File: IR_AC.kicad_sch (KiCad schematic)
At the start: 1 part

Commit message: late night work on led current
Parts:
- added C1, C2: 1u, Capacitor_SMD:C_0603_1608Metric, symbol Device:C
- added CLDO1, CLDO2: 1u, Capacitor_SMD:C_0805_2012Metric, symbol Device:C
- added D1: 1N5819HW, LC_libz_foot:1N5819HW, symbol Device:D_Schottky
- added D2, D3: RED_GREEN, LED_SMD:LED_0805_2012Metric, symbol Device:LED
- added D4: LED, LC_libz_foot:IR_LED_TH_5MM, symbol Device:LED
- added D5: RED, LED_SMD:LED_0805_2012Metric, symbol Device:LED
- added H1, H2, H3, H4: MountingHole, MountingHole:MountingHole_3.2mm_M3, symbol Mechanical:MountingHole
- added J1: TYPE-C 16PIN 2MD(073), LC_libz_foot:USB-C-SMD_TYPE-C-6PIN-2MD-073, symbol LC_libz_sym:TYPE-C16PIN2MD(073)
- added Q1: NMOS, Package_TO_SOT_SMD:SOT-23, symbol Simulation_SPICE:NMOS
- added R2: 10k, Resistor_SMD:R_0603_1608Metric, symbol Device:R
- added R3: 100R, Resistor_SMD:R_0603_1608Metric, symbol Device:R
- added R4: 100k, Resistor_SMD:R_0603_1608Metric, symbol Device:R
- added R?: 3k3, Resistor_SMD:R_0603_1608Metric, symbol Device:R
- added R?: 220R, Resistor_SMD:R_0603_1608Metric, symbol Device:R
- added R?: 820R, Resistor_SMD:R_0603_1608Metric, symbol Device:R
- added R?: 33R, Resistor_SMD:R_1206_3216Metric, symbol Device:R
- added RCC1, RCC2: 5.1k, Resistor_SMD:R_0603_1608Metric, symbol Device:R
- added SW1, SW2: SW_Push, LC_libz_foot:BTN_L45_W45, symbol Switch:SW_Push
- added TP1, TP2, TP3: TestPoint, TestPoint:TestPoint_THTPad_D1.5mm_Drill0.7mm, symbol Connector:TestPoint
- added U1: AP2112K-3.3TRG1, LC_libz_foot:AP2112K-3.3, symbol LC_libz_sym:AP2112K-3.3TRG1
- added U2: WS2812B_5050, LC_libz_foot:WS2812B_5050, symbol LC_libz_sym:WS2812B_5050
- added U3: ESP32-S3-WROOM-1, RF_Module:ESP32-S3-WROOM-1, symbol RF_Module:ESP32-S3-WROOM-1
- R1: LCSC C2930027 -> C25804
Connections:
- net +5V: now also CLDO1.1, D1.1 (K), R?.2, R?.2, R?.2, U1.1 (VIN), U1.3 (EN); no longer R1.1
- net GND: now also C1.2, C2.2, CLDO1.2, CLDO2.2, D2.1 (K), D3.1 (K), J1.1 (GND), J1.12 (GND), Q1.3 (S), R4.1, RCC1.1, RCC2.1, SW1.1, SW2.1, U1.2 (GND), U2.3 (GND), U3.1 (GND), U3.40 (GND), U3.41 (GND); no longer R1.2
- new net: D3.2 (A), R?.1, TP2.1
- new net: D5.2 (A), R?.1
- new net: D2.2 (A), R?.1, TP1.1
- new net: J1.10 (CC2), RCC2.2
- new net: J1.4 (CC1), RCC1.2
- new net: D4.1 (K), D5.1 (K), Q1.1 (D)
- new net: Q1.2 (G), R3.1, R4.2
- new net: D4.2 (A), R?.1, TP3.1
- new net +3V3: CLDO2.1, R1.2, R2.2, R?.2, U1.5 (VOUT), U3.2 (3V3)
- new net BOOT: C2.1, R2.1, SW2.2, U3.27 (IO0)
- new net D+: J1.6 (DP1), J1.8 (DP2), U3.14 (USB_D+)
- new net D-: J1.5 (DN2), J1.7 (DN1), U3.13 (USB_D-)
- new net EN: C1.1, R1.1, SW1.2, U3.3 (EN)
- new net IR_LED_DRIVE: R3.2
- new net LED_STATUS: U2.1 (VDD)
- new net VDC: D1.2 (A), J1.11 (VBUS), J1.2 (VBUS)
- no-connect marks 0 -> 6
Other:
- note added: "Assuming IR LED pulses of 100mA, the R_DS(on) of the NMOS (2N7002) will cause a V_DS drop of ~0.4V. At this current the IR LED will drop about 1.3V. Hence, the current- limiting resistor is calculated as: R_IR-LED = (5-1.3-0.4)/0.1 = 33R ..and power P = (0.1)^2 * (33) = 0.33 W => 1206"
- note added: "EN-RESET / BOOT BUTTONS"
- note added: "Fixed 3V3 LDO (efficient, not monolithic AMS1117)"
- note added: "Hence, more like 4.55V"
- note added: "IR Blaster"
- note added: "IR TX LED (940nm) 5mm THT"
- note added: "Ideally differentially routed but only short. Z_0 = 90R."
- note added: "Indicator LEDs"
- note added: "Mounting Holes"
- note added: "Schottky reverse polarity protection"
- note added: "Strapping pins copied from ESP32-S3 DevKitC-1 schematic"
- note added: "Tandem visible spectrum LED to indicate TX"
- note added: "USB-C 16P Receptacle (power + data)"
- note added: "V_F = 0.45V @ 1A"
- note added: "WS2812B RGB Status LED"

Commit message: Finished schematic
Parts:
- added C1, C4: 10u, Capacitor_SMD:C_0805_2012Metric, symbol Device:C
- added C5: 100n, Capacitor_SMD:C_0402_1005Metric, symbol Device:C
- added D4: YELLOW, LED_SMD:LED_0805_2012Metric, symbol Device:LED
- added J2: Conn_01x04_Pin, libs:HDR-TH_4P-P2.54-V-M, symbol Connector:Conn_01x04_Pin
- added R3: 1k, Resistor_SMD:R_0603_1608Metric, symbol Device:R
- added TP3: TestPoint, TestPoint:TestPoint_THTPad_D1.5mm_Drill0.7mm, symbol Connector:TestPoint
- added U2: USBLC6-4, Package_TO_SOT_SMD:SOT-23-6, symbol Power_Protection:SRV05-4
- D2, D3: value RED_GREEN -> GREEN
- D6: renamed from D5; LCSC NULL -> C84256
- H1, H2, H3, H4: footprint MountingHole:MountingHole_3.2mm_M3 -> MountingHole:MountingHole_2.2mm_M2
- J1: footprint LC_libz_foot:USB-C-SMD_TYPE-C-6PIN-2MD-073 -> libs:USB-C-SMD_TYPE-C-6PIN-2MD-073
- R1: renamed from R?; value 220R -> 680R; LCSC C22962 -> C23228
- R2: renamed from R?; value 820R -> 2k2; LCSC C23253 -> C4190
- R6: renamed from R?; value 33R -> 30R; LCSC C18005 -> C25373
- R7: renamed from R?; value 3k3 -> 330R; LCSC C22978 -> C23138
- SW1, SW2: footprint LC_libz_foot:BTN_L45_W45 -> (none); LCSC C455243 -> C720477
- U1: footprint LC_libz_foot:AP2112K-3.3 -> libs:SOT-25-5_L2.9-W1.6-P0.95-LS2.8-BL
- renumbered CLDO1 to C2, CLDO2 to C3, C1 to C6, C2 to C7, D4 to D5, R1 to R4, R2 to R5, R3 to R8, R4 to R9, TP3 to TP4, U2 to U3, U3 to U4
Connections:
- net +5V is gone; now on net VDC: C2.1, D1.1 (K), R2.2, R6.2, R7.2, U1.1 (VIN), U1.3 (EN)
- net +3V3: now also TP1.1, C4.1, C5.1, J2.1 (Pin_1)
- net D+: now also U2.3 (S2)
- net D-: now also U2.4 (S3)
- net GND: now also J1.13 (SHELL), J1.14 (SHELL), C1.2, C4.2, C5.2, D4.1 (K), J2.4 (Pin_4), U2.2 (GND)
- net IR_LED_DRIVE: now also U4.21 (IO13)
- net LED_STATUS: now also U3.4 (DIN), U4.20 (IO12); no longer U3.1 (VDD)
- net VDC: now also TP2.1, U3.1 (VDD), C1.1; no longer D1.2 (A), J1.11 (VBUS), J1.2 (VBUS)
- net at D3.2 (A), R2.1: no longer TP2.1
- net at D2.2 (A), R1.1: no longer TP1.1
- net CC2: now reaches J1.10 (CC2), RCC2.2
- net CC2: now also U2.1 (S1)
- net CC1: now reaches J1.4 (CC1), RCC1.2
- net CC1: now also U2.6 (S4)
- net DEBUG: now reaches U4.22 (IO14)
- net DEBUG: now also R3.2, TP3.1
- net RX: now reaches U4.36 (RXD0)
- net RX: now also J2.3 (Pin_3)
- net TX: now reaches U4.37 (TXD0)
- net TX: now also J2.2 (Pin_2)
- new net: D4.2 (A), R3.1
- new net V_BUS: D1.2 (A), J1.11 (VBUS), J1.2 (VBUS), U2.5 (VBUS)
- no-connect marks 6 -> 32
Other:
- note added: "Assuming IR LED pulses of 100mA, the R_DS(on) of the NMOS (2N7002) will cause a V_DS drop of ~0.4V. At this current the IR LED will drop about 1.3V. Hence, the current- limiting resistor is calculated as: R_IR-LED = (5-1.3-0.4)/0.1 = 30R ..and power P = (0.1)^2 * (30) = 0.30 W => 1206"
- note added: "BOOT"
- note added: "Bit of bulk"
- note added: "Debug LED / TP"
- note added: "ESD Protection diode array"
- note added: "Hence, more like 4.7 V"
- note added: "IR TX LED (940nm) 5mm THT Oriented towards AC IR receiver"
- note added: "Ideally impedance controlled,but only short. Z_0 = 90R."
- note added: "Microcontroller"
- note added: "RESET"
- note added: "Request 5V (up to 3A) sink"
- note added: "UART"
- note added: "V_F = 0.3 V @ 100 mA"
- note added: "~0.9 mA"
- note added: "~1.1 mA"
- note added: "~4V7"
- note removed: "Assuming IR LED pulses of 100mA, the R_DS(on) of the NMOS (2N7002) will cause a V_DS drop of ~0.4V. At this current the IR LED will drop about 1.3V. Hence, the current- limiting resistor is calculated as: R_IR-LED = (5-1.3-0.4)/0.1 = 33R ..and power P = (0.1)^2 * (33) = 0.33 W => 1206"
- note removed: "Hence, more like 4.55V"
- note removed: "IR TX LED (940nm) 5mm THT"
- note removed: "Ideally differentially routed but only short. Z_0 = 90R."
- note removed: "V_F = 0.45V @ 1A"
- moved on the sheet: C2, C3, C6, C7, D1, D2, D3, D5, D6, H1, J1, Q1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

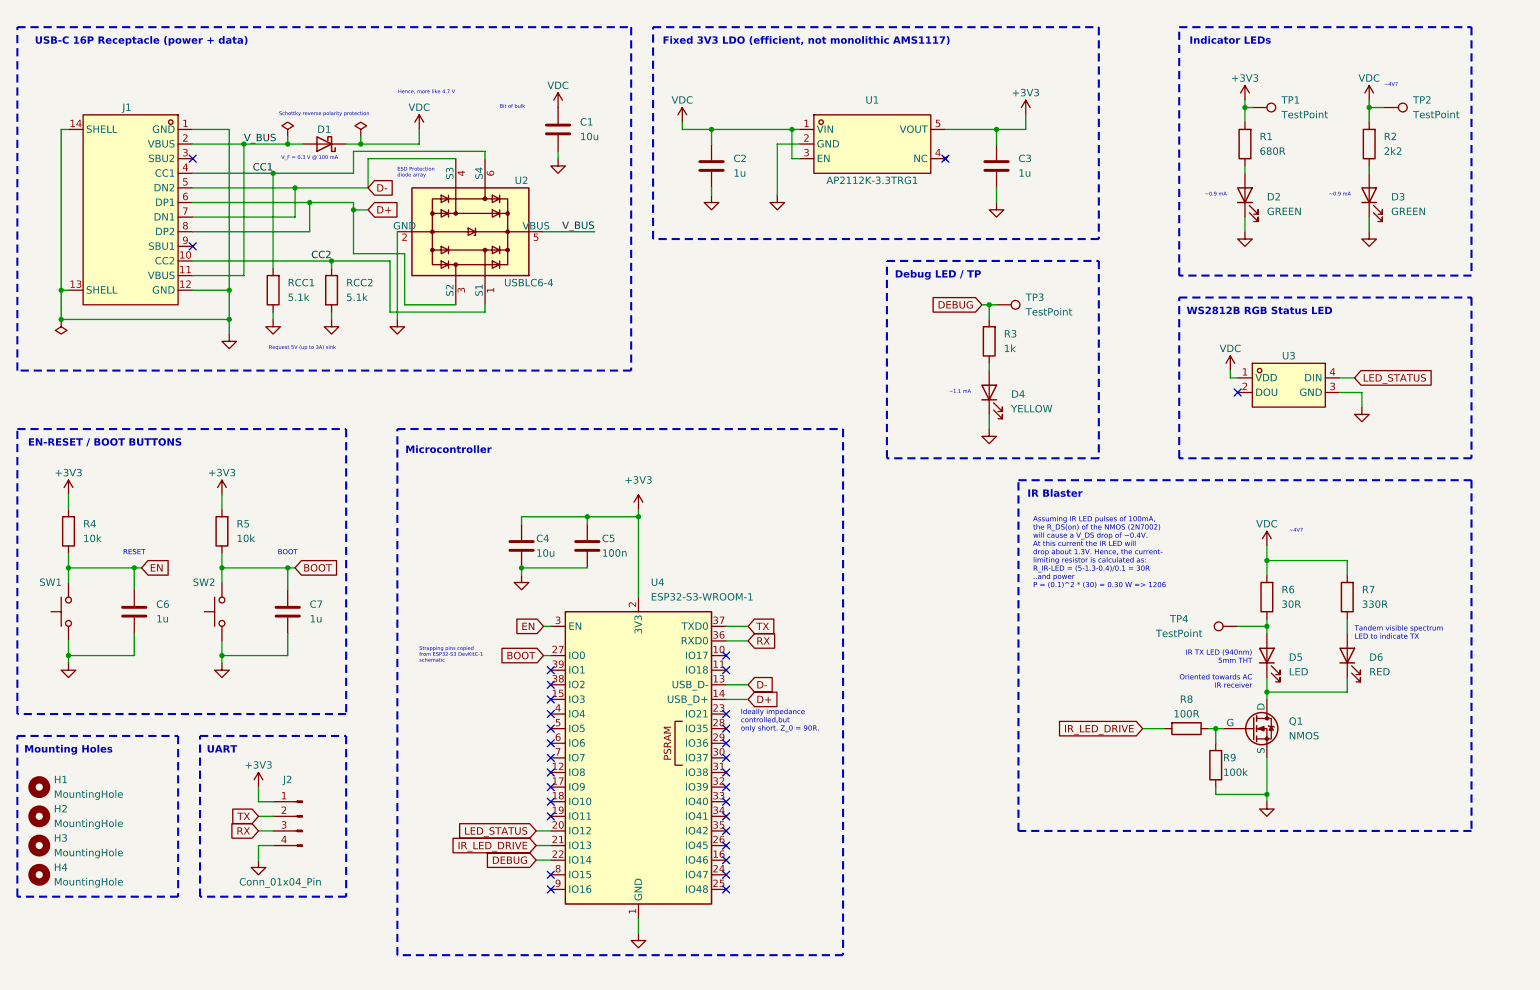
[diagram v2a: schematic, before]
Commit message: Routing + DRC complete. Ordered with JLCPCB + LCSC
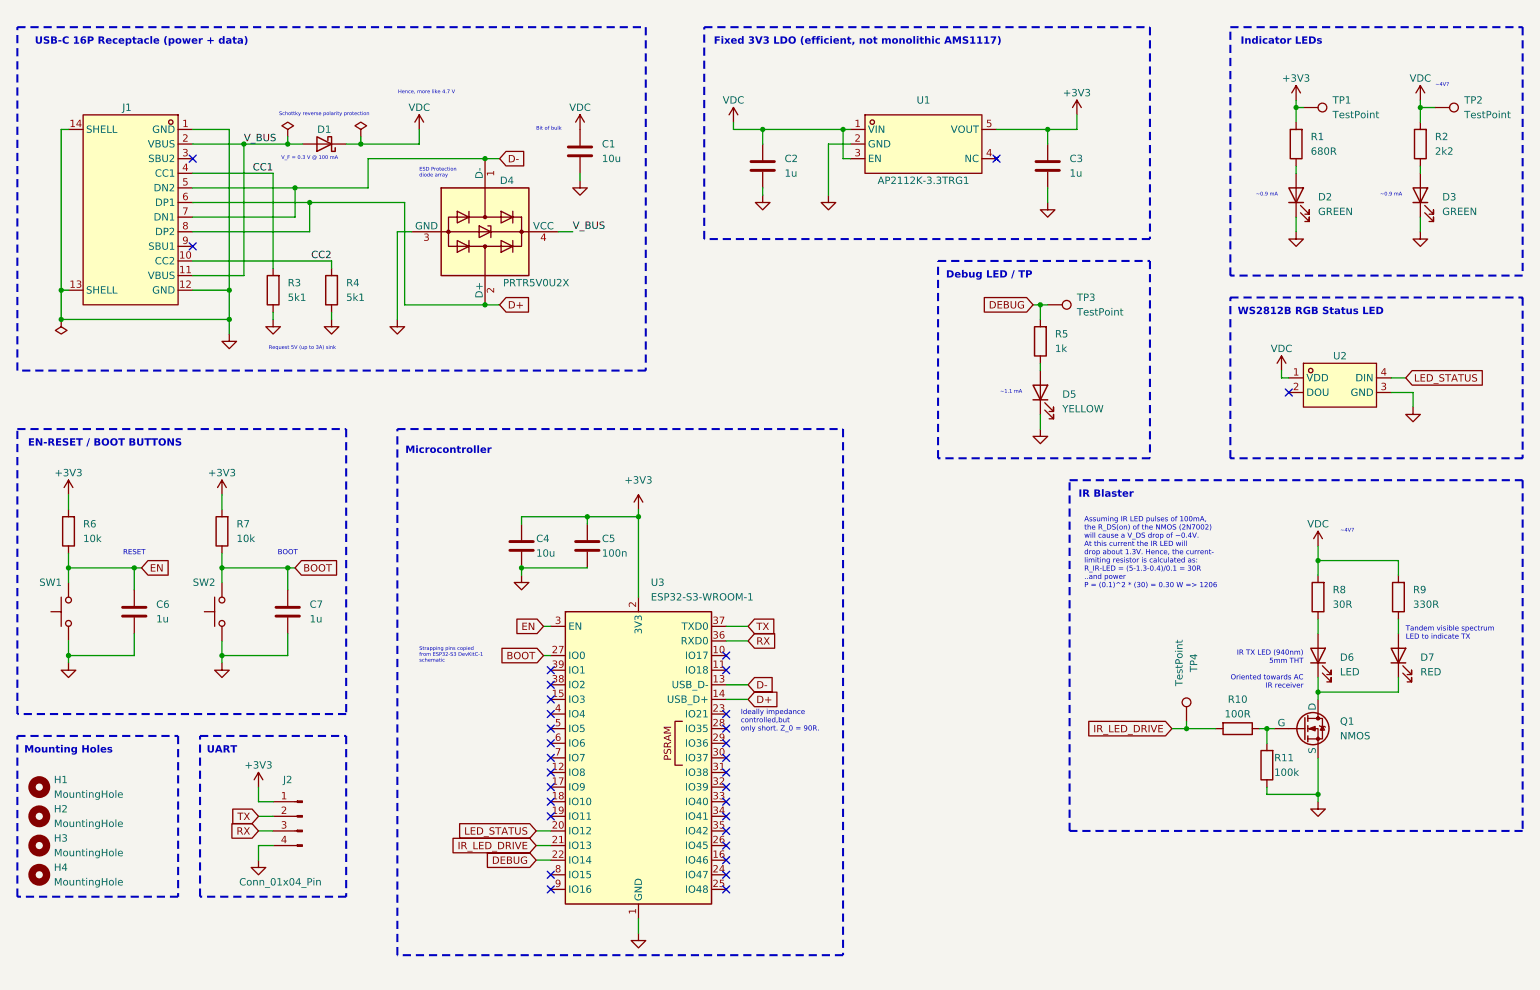
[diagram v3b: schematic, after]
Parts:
- removed RCC2: 5.1k, Resistor_SMD:R_0603_1608Metric, symbol Device:R
- removed U2: USBLC6-4, Package_TO_SOT_SMD:SOT-23-6, symbol Power_Protection:SRV05-4
- added D4: PRTR5V0U2X, libs:SOT-666-6_L1.6-W1.2-P0.50-LS1.6-BR, symbol Power_Protection:PRTR5V0U2X
- added R4: 5k1, Resistor_SMD:R_0402_1005Metric, symbol Device:R
- R3: renamed from RCC1; value 5.1k -> 5k1; footprint Resistor_SMD:R_0603_1608Metric -> Resistor_SMD:R_0402_1005Metric; LCSC C23186 -> C25905
- SW1, SW2: footprint (none) -> libs:SW-SMD_L3.9-W3.0-P4.45
- renumbered D4 to D5, D5 to D6, D6 to D7, R8 to R10, R9 to R11, R3 to R5, R4 to R6, R5 to R7, R6 to R8, R7 to R9, U3 to U2, U4 to U3
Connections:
- net CC2: now also R4.2
- net D+: now also D4.2 (D+)
- net D-: now also D4.1 (D-)
- net GND: now also D4.3 (GND), R4.1
- net IR_LED_DRIVE: now also TP4.1
- net V_BUS: now also D4.4 (VCC)
- net at D6.2 (A), R8.1: no longer TP4.1
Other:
- moved on the sheet: C1, C2, C3, D2, D3, D5, D6, D7, Q1, R1, R10, R11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
